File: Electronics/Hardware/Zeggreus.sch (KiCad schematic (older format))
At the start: 113 parts, among them J1 USB_B_Micro, J10 SMA, J13 USART1, J14 PC5, J2 Batt, J3 Servo1, J4 Servo2, J5 Servo3, J6 Servo4, J7 Micro_SD_Card_TF-15×15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

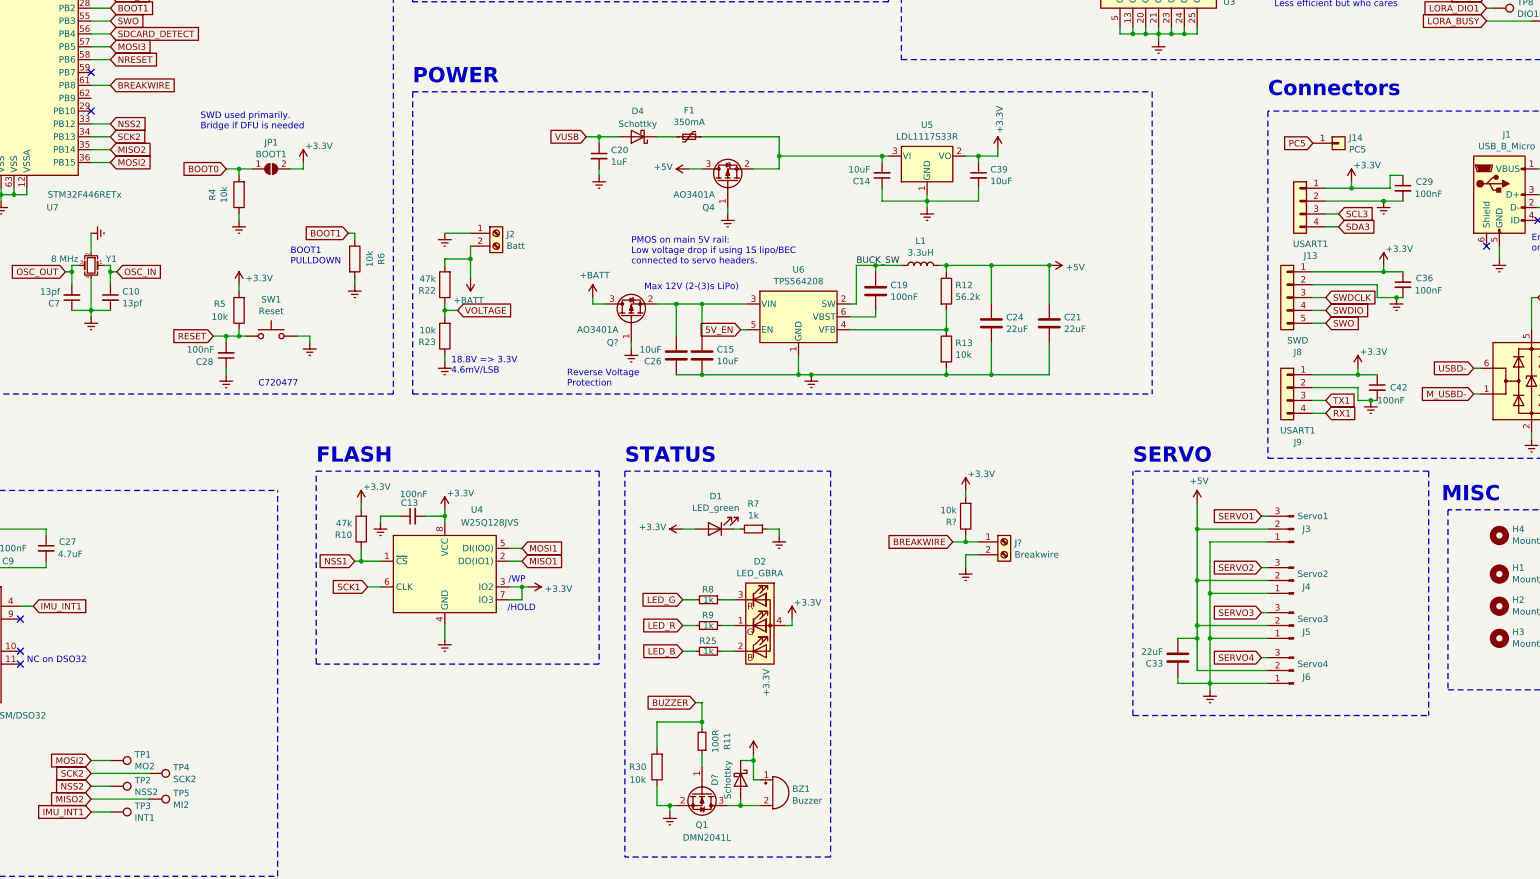
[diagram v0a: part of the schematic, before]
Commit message: Antenna model and PCB tweaks
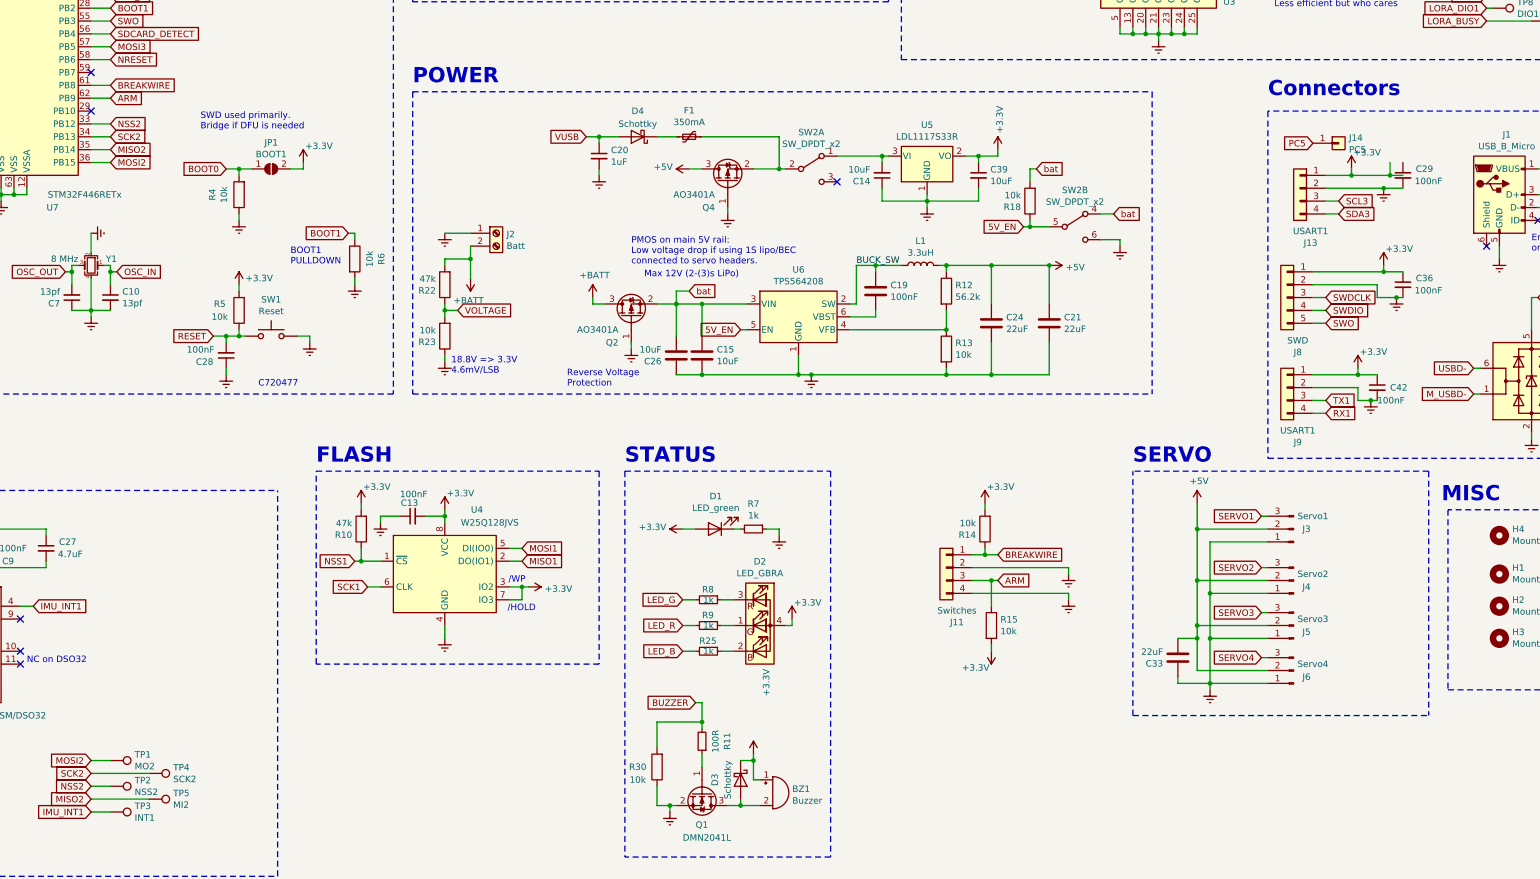
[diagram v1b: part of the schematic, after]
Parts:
- removed J?: Breakwire, starling:TerminalBlock_4Ucon_1x02_P3.50mm_Horizontal_blue, symbol Connector:Screw_Terminal_01x02
- added J11: Switches, Connector_PinHeader_2.54mm:PinHeader_1x04_P2.54mm_Vertical, symbol Connector_Generic:Conn_01x04
- added R15, R18: 10k, Resistor_SMD:R_0603_1608Metric, symbol Device:R
- added SW2: SW_DPDT_x2, starling:SW_DPDT_MST22D18G2, symbol Switch:SW_DPDT_x2
- gave numbers to parts that had none: 3
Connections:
- net +3V3: now also R15.2; no longer C29.1
- net 5V_EN: now also R18.1, SW2.5 (B)
- net BREAKWIRE: now also J11.1 (Pin_1)
- net Earth: now also J11.2 (Pin_2), J11.4 (Pin_4), SW2.6 (C)
- net at C14.2, U5.3 (VI): now also SW2.1 (A); no longer F1.1, Q4.2 (S)
- net bat: now reaches C15.1, C26.2, Q2.2 (S), U6.3 (VIN)
- net bat: now also R18.2, SW2.4 (A)
- net ARM: now reaches U7.62 (PB9)
- net ARM: now also J11.3 (Pin_3), R15.1
- new net: F1.1, Q4.2 (S), SW2.2 (B)
- no-connect marks 14 -> 15
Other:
- moved on the sheet: C29, J13, R14

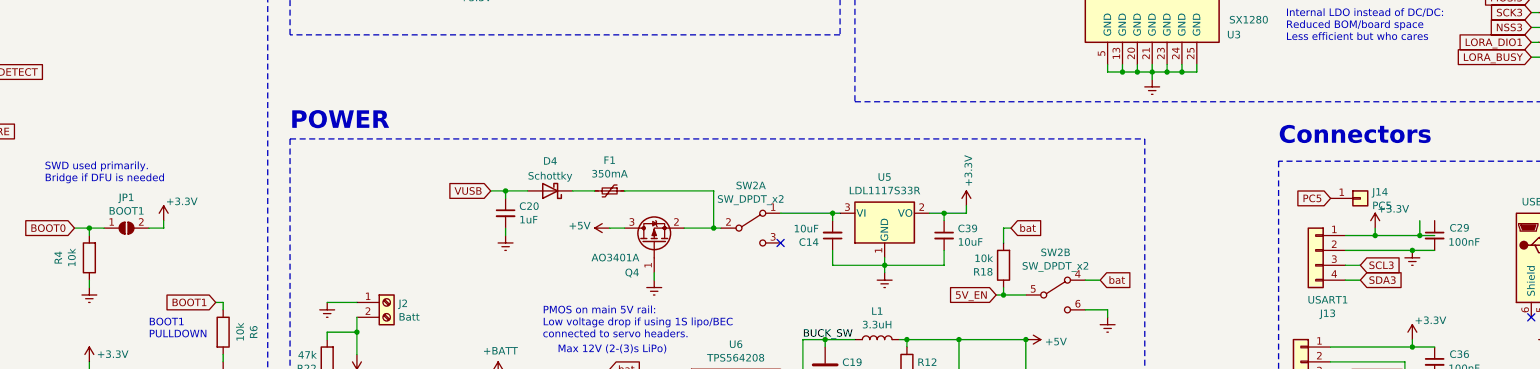
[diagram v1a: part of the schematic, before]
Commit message: update electronics and added camera model
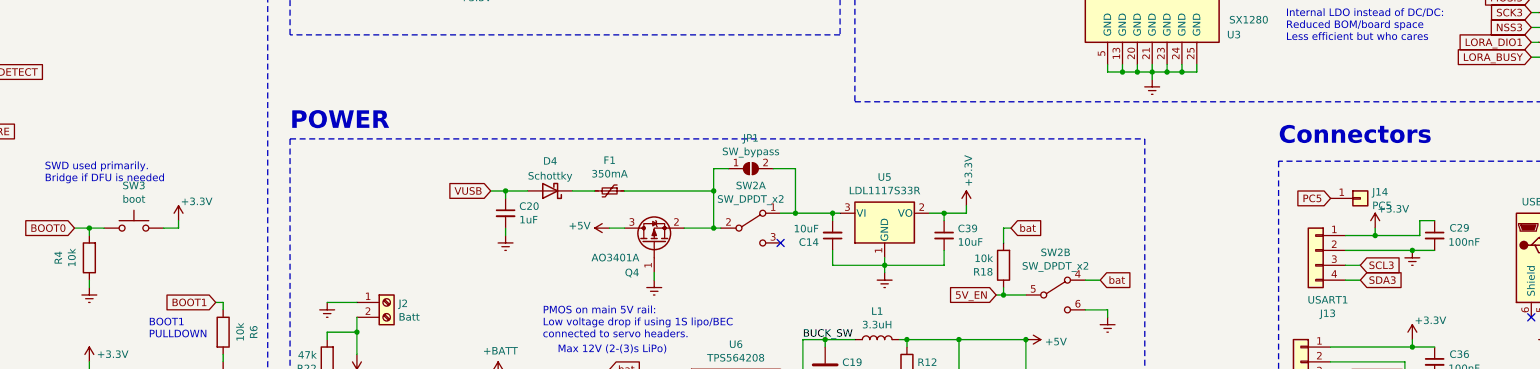
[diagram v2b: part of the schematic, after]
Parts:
- added SW3: boot, starling:SW_Push_SPST_3×4×2, symbol Switch:SW_Push
- JP1: value BOOT1 -> SW_bypass
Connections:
- net +3V3: now also C29.1, SW3.2; no longer JP1.2 (B)
- net BOOT0: now also SW3.1; no longer JP1.1 (A)
- net at C14.2, SW2.1 (A), U5.3 (VI): now also JP1.2 (B)
- net at F1.1, Q4.2 (S), SW2.2 (B): now also JP1.1 (A)
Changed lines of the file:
@@
 L power:+3.3V #PWR025
 U 1 1 5F04ADA4
-P 5500 5600
-F 0 "#PWR025" H 5500 5450 50  0001 C CNN
-F 1 "+3.3V" H 5515 5728 50  0000 L CNN
-F 2 "" H 5500 5600 50  0001 C CNN
-F 3 "" H 5500 5600 50  0001 C CNN
-	1    5500 5600
+P 5600 5600
+F 0 "#PWR025" H 5600 5450 50  0001 C CNN
+F 1 "+3.3V" H 5615 5728 50  0000 L CNN
+F 2 "" H 5600 5600 50  0001 C CNN
+F 3 "" H 5600 5600 50  0001 C CNN
+	1    5600 5600
 	1    0    0    -1
 $EndComp
@@
 Connection ~ 7800 5400
 Wire Wire Line
-	5500 5600 5500 5650
-Wire Wire Line
-	5500 5650 5400 5650
+	5600 5600 5600 5650
+Wire Wire Line
+	5600 5650 5500 5650
 Text GLabel 8450 9000 0    50   Input ~ 0
 LED_G
@@
 Text Notes 13050 4400 0    50   ~ 0
 Internal LDO instead of DC/DC:\nReduced BOM/board space\nLess efficient but who cares
-$Comp
-L Jumper:SolderJumper_2_Open JP1
-U 1 1 6110A6BC
-P 5250 5650
-F 0 "JP1" H 5250 5855 50  0000 C CNN
-F 1 "BOOT1" H 5250 5764 50  0000 C CNN
-F 2 "Jumper:SolderJumper-2_P1.3mm_Open_RoundedPad1.0x1.5mm" H 5250 5650 50  0001 C CNN
-F 3 "~" H 5250 5650 50  0001 C CNN
-	1    5250 5650
-	1    0    0    -1
-$EndComp
 Text Notes 4700 5350 0    50   ~ 0
 SWD used primarily.\nBridge if DFU is needed
@@
 Wire Wire Line
 	13950 5700 13950 5600
-Wire Wire Line
-	13950 5700 14050 5700
 Connection ~ 13650 5700
 $Comp
@@
 Text Notes 7550 7350 0    50   ~ 0
 Reverse Voltage\nProtection
-Connection ~ 13950 5700
 $Comp
 L Connector_Generic:Conn_01x04 J11
@@
 NoConn ~ 9650 5750
 Wire Wire Line
-	9650 5550 10000 5550
+	9650 5550 9750 5550
 Connection ~ 10000 5550
 Wire Wire Line
@@
 Wire Wire Line
 	11150 5650 11200 5650
+$Comp
+L Switch:SW_Push SW3
+U 1 1 60415EC8
+P 5300 5650
+F 0 "SW3" H 5300 5935 50  0000 C CNN
+F 1 "boot" H 5300 5844 50  0000 C CNN
+F 2 "starling:SW_Push_SPST_3×4×2" H 5300 5850 50  0001 C CNN
+F 3 "~" H 5300 5850 50  0001 C CNN
+F 4 "C720477" H 5300 5650 50  0001 C CNN "LCSC"
+	1    5300 5650
+	1    0    0    -1
+$EndComp
+Wire Wire Line
+	13950 5600 14050 5600
+$Comp
+L Jumper:SolderJumper_2_Open JP1
+U 1 1 6073245B
+P 9450 5250
+F 0 "JP1" H 9450 5455 50  0000 C CNN
+F 1 "SW_bypass" H 9450 5364 50  0000 C CNN
+F 2 "Jumper:SolderJumper-2_P1.3mm_Open_RoundedPad1.0x1.5mm" H 9450 5250 50  0001 C CNN
+F 3 "~" H 9450 5250 50  0001 C CNN
+	1    9450 5250
+	1    0    0    -1
+$EndComp
+Wire Wire Line
+	9300 5250 9200 5250
+Wire Wire Line
+	9200 5250 9200 5400
+Connection ~ 9200 5400
+Wire Wire Line
+	9600 5250 9750 5250
+Wire Wire Line
+	9750 5250 9750 5550
+Connection ~ 9750 5550
+Wire Wire Line
+	9750 5550 10000 5550
 $EndSCHEMATC
